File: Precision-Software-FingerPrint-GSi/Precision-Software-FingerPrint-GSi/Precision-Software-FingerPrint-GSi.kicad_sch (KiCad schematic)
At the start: 42 parts, among them J1 Conn_01x03_Pin, J2 Bus_Apple_II_Card_Side, SW1 SW_DIP_x08, U1 G65SC02P-1, U10 PAL10L8CN, U11 PAL10L8CN, U12 74LS374, U13 74LS05, U14 74LS74, U15 74LS279, U16 74LS367, U2 HM6264P-15, U3 27512, U4 27512, U5 74LS374, U6 74LS374, U7 74LS374, U8 74LS374, U9 74LS374

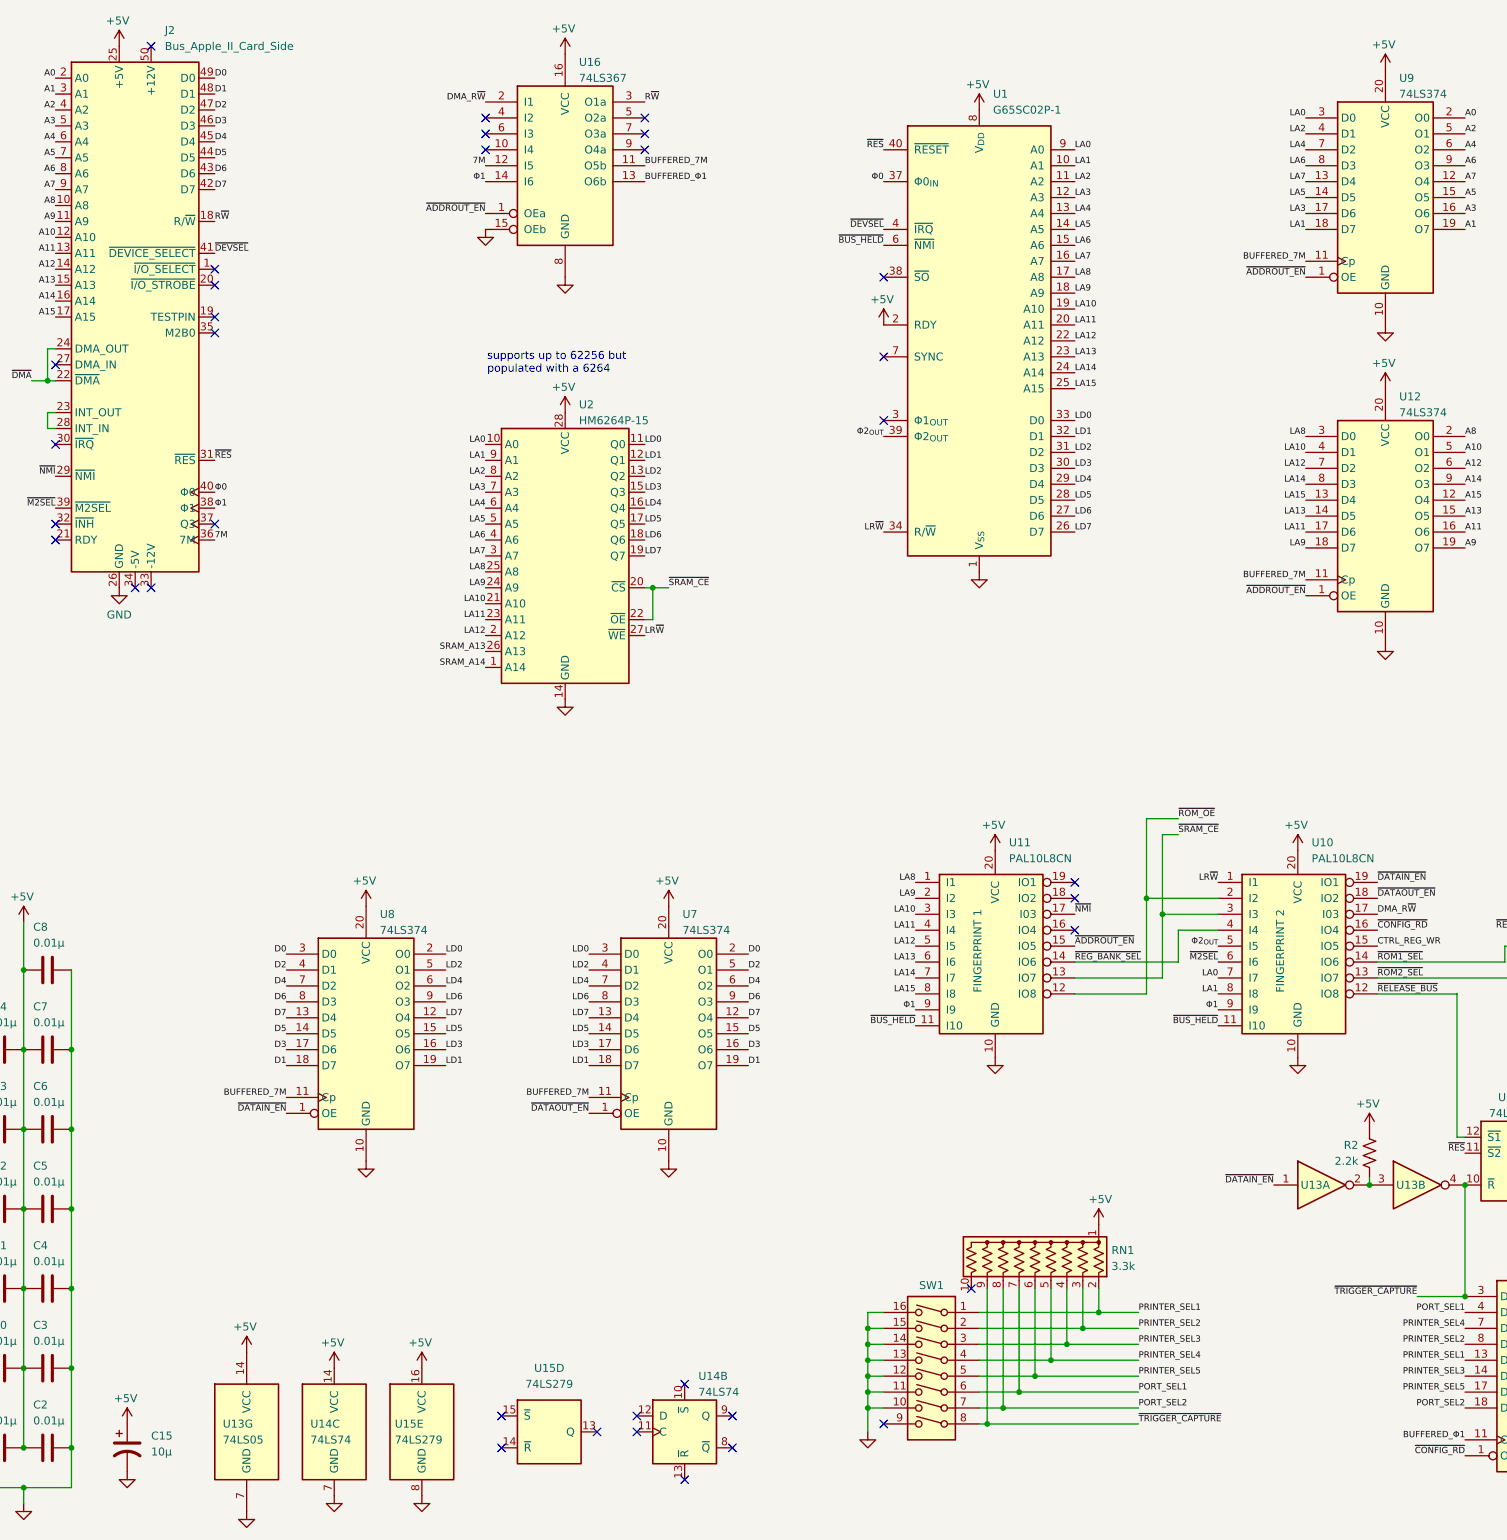
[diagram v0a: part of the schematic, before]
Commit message: Create a better PAL10L8 symbol
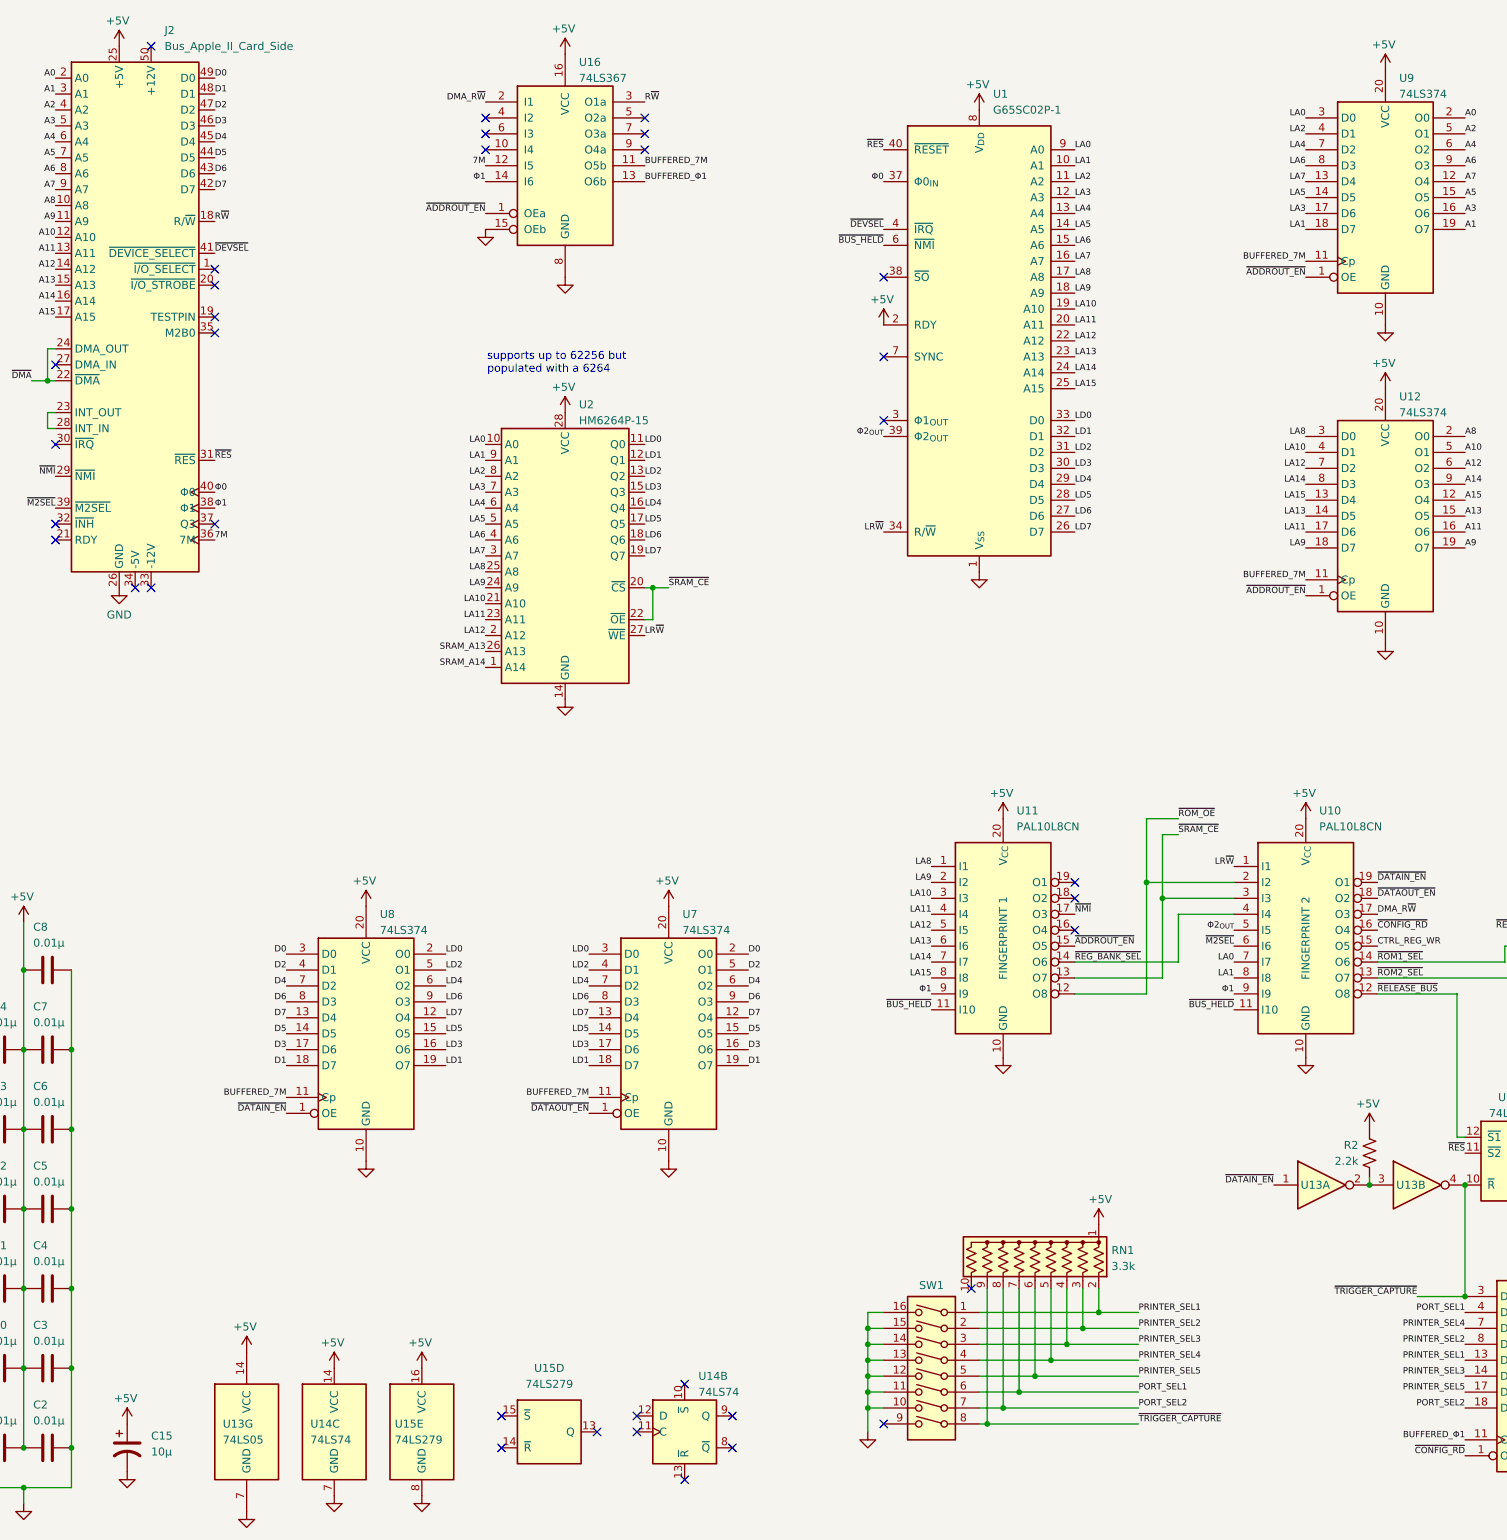
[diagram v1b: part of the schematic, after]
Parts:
- removed U10, U11: PAL10L8CN, symbol Logic_Programmable:PAL16L8
- added U10, U11: PAL10L8CN, Package_DIP:DIP-20_W7.62mm, symbol Logic_Legacy:PAL10L8
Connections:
- net +5V: now also U10.20 (V_{CC}), U11.20 (V_{CC})
- net CTRL_REG_WR: now also U10.15 (O5)
- net DMA_R~{W}: now also U10.17 (O3)
- net GND: now also U10.10 (GND), U11.10 (GND)
- net LA0: now also U10.7 (I7)
- net LA1: now also U10.8 (I8)
- net LA10: now also U11.3 (I3)
- net LA11: now also U11.4 (I4)
- net LA12: now also U11.5 (I5)
- net LA13: now also U11.6 (I6)
- net LA14: now also U11.7 (I7)
- net LA15: now also U11.8 (I8)
- net LA8: now also U11.1 (I1)
- net LA9: now also U11.2 (I2)
- net LR~{W}: now also U10.1 (I1)
- net ~{ADDROUT_EN}: now also U11.15 (O5)
- net ~{BUS_HELD}: now also U10.11 (I10), U11.11 (I10)
- net ~{CONFIG_RD}: now also U10.16 (O4)
- net ~{DATAIN_EN}: now also U10.19 (O1)
- net ~{DATAOUT_EN}: now also U10.18 (O2)
- net ~{M2SEL}: now also U10.6 (I6)
- net ~{NMI}: now also U11.17 (O3)
- net ~{REG_BANK_SEL}: now also U10.4 (I4), U11.14 (O6)
- net ~{RELEASE_BUS}: now also U10.12 (O8)
- net ~{ROM1_SEL}: now also U10.14 (O6)
- net ~{ROM2_SEL}: now also U10.13 (O7)
- net ~{ROM_OE}: now also U10.2 (I2), U11.12 (O8)
- net ~{SRAM_CE}: now also U10.3 (I3), U11.13 (O7)
- net Φ1: now also U10.9 (I9), U11.9 (I9)
- net Φ2_{OUT}: now also U10.5 (I5)
